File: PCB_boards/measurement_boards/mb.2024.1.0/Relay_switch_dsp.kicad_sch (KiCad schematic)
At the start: 8 parts, among them K1 G5LE-1, K2 G5LE-1, Q1 ZVN4206ASTZ, Q2 ZVN4206ASTZ

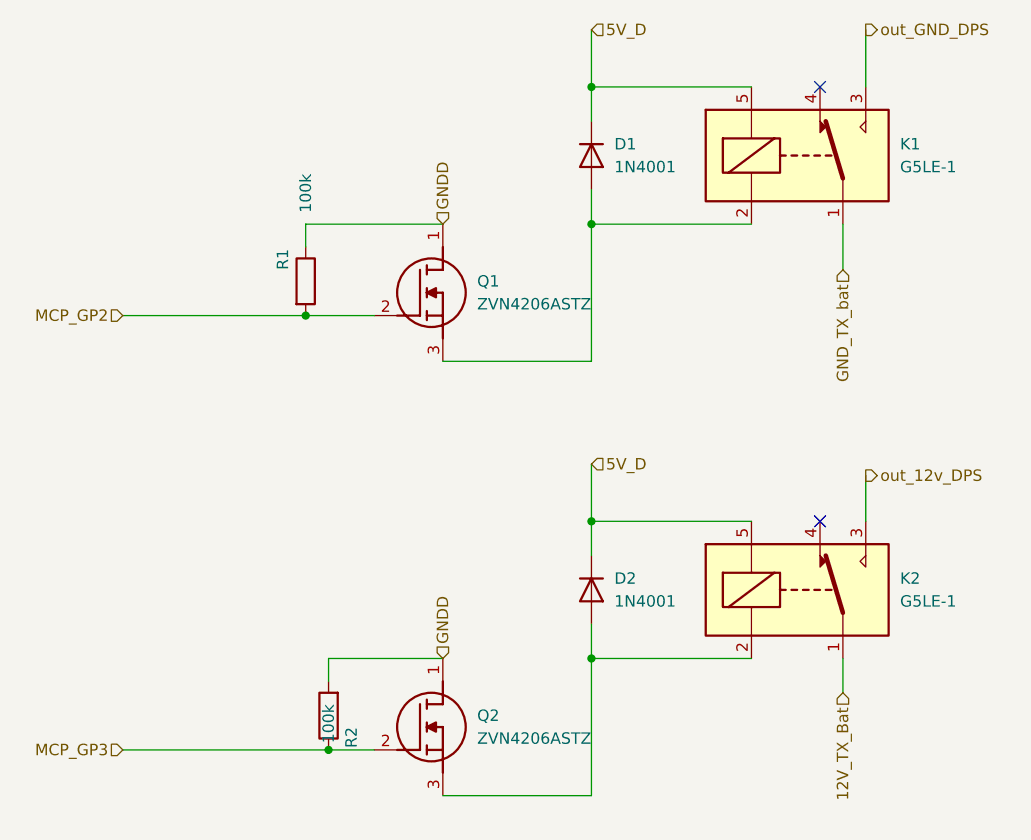
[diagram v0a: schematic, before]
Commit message: update diode 1n4007
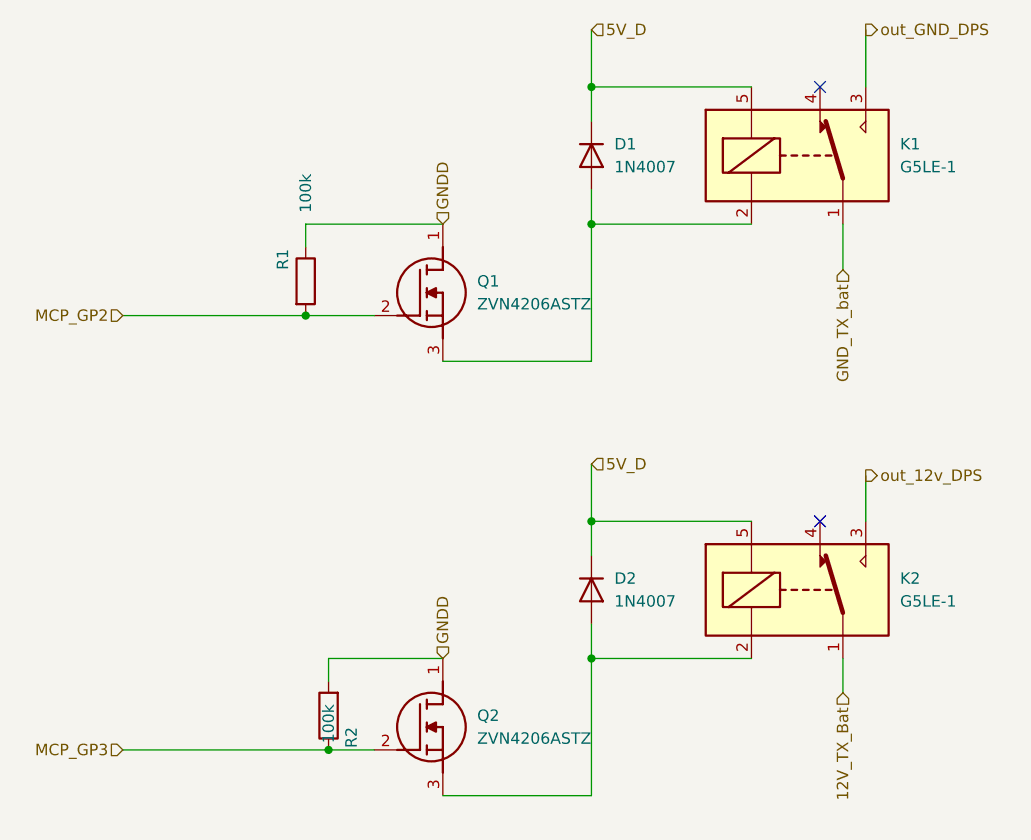
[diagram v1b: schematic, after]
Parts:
- D1, D2: value 1N4001 -> 1N4007
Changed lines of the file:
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@@
     (pin "3")
     (instances
-      (project "mb.2024.0.3"
+      (project "mb.2024.1.0"
         (path "/62d2b953-c7cc-4d07-805d-38225011d95a/433fb79c-38b7-4d80-8278-5eb2a5e83393"
           (reference "Q2") (unit 1)
@@
     (pin "5")
     (instances
-      (project "mb.2024.0.3"
+      (project "mb.2024.1.0"
         (path "/62d2b953-c7cc-4d07-805d-38225011d95a/433fb79c-38b7-4d80-8278-5eb2a5e83393"
           (reference "K1") (unit 1)
@@
     (pin "5")
     (instances
-      (project "mb.2024.0.3"
+      (project "mb.2024.1.0"
         (path "/62d2b953-c7cc-4d07-805d-38225011d95a/433fb79c-38b7-4d80-8278-5eb2a5e83393"
           (reference "K2") (unit 1)
@@
       (effects (font (size 1.27 1.27)) (justify left))
     )
-    (property "Value" "1N4001" (at 118.11 114.3 90)
+    (property "Value" "1N4007" (at 118.11 114.3 90)
       (effects (font (size 1.27 1.27)) (justify left))
     )
@@
     (pin "2")
     (instances
-      (project "mb.2024.0.3"
+      (project "mb.2024.1.0"
         (path "/62d2b953-c7cc-4d07-805d-38225011d95a/433fb79c-38b7-4d80-8278-5eb2a5e83393"
           (reference "D2") (unit 1)
@@
     (pin "3")
     (instances
-      (project "mb.2024.0.3"
+      (project "mb.2024.1.0"
         (path "/62d2b953-c7cc-4d07-805d-38225011d95a/433fb79c-38b7-4d80-8278-5eb2a5e83393"
           (reference "Q1") (unit 1)
@@
       (effects (font (size 1.27 1.27)) (justify left))
     )
-    (property "Value" "1N4001" (at 118.11 66.04 90)
+    (property "Value" "1N4007" (at 118.11 66.04 90)
       (effects (font (size 1.27 1.27)) (justify left))
     )
@@
     (pin "2")
     (instances
-      (project "mb.2024.0.3"
+      (project "mb.2024.1.0"
         (path "/62d2b953-c7cc-4d07-805d-38225011d95a/433fb79c-38b7-4d80-8278-5eb2a5e83393"
           (reference "D1") (unit 1)
@@
     (pin "2")
     (instances
-      (project "mb.2024.0.3"
+      (project "mb.2024.1.0"
         (path "/62d2b953-c7cc-4d07-805d-38225011d95a/433fb79c-38b7-4d80-8278-5eb2a5e83393"
           (reference "R1") (unit 1)
@@
     (pin "2")
     (instances
-      (project "mb.2024.0.3"
+      (project "mb.2024.1.0"
         (path "/62d2b953-c7cc-4d07-805d-38225011d95a/433fb79c-38b7-4d80-8278-5eb2a5e83393"
           (reference "R2") (unit 1)
